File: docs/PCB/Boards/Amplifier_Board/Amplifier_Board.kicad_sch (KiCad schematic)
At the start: 16 parts, among them IC1 LM4871MX_NOPB, J2 Barrel_Jack

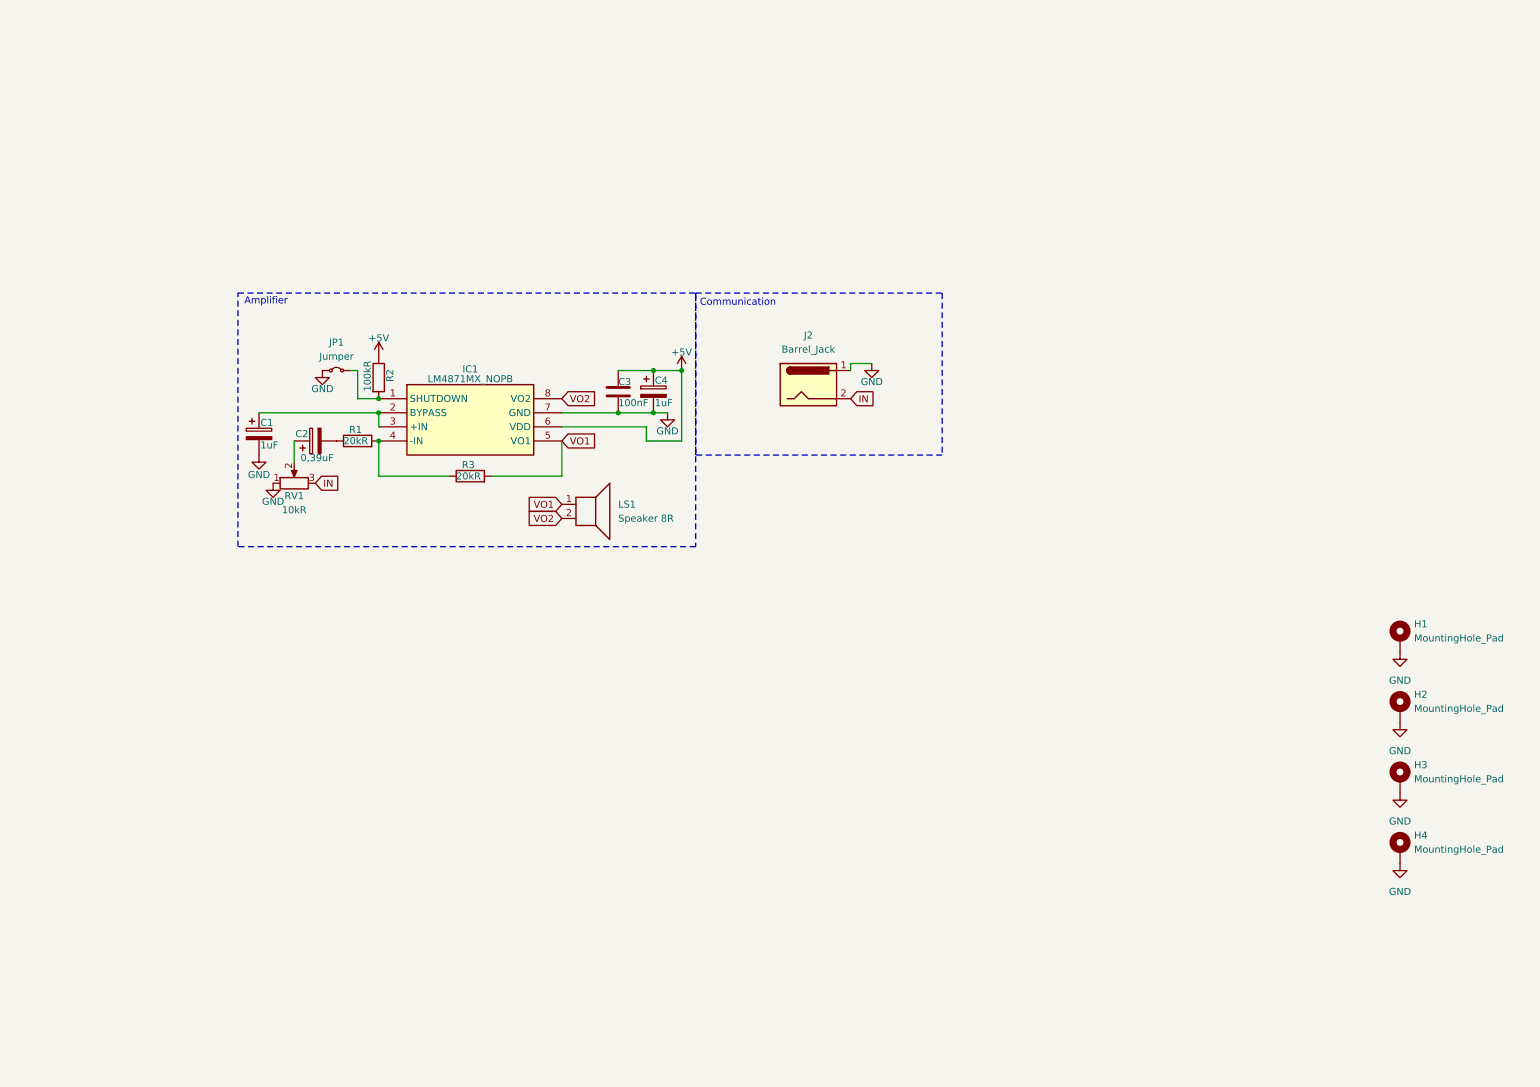
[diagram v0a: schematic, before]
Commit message: Boards modified - tree and power boards added.
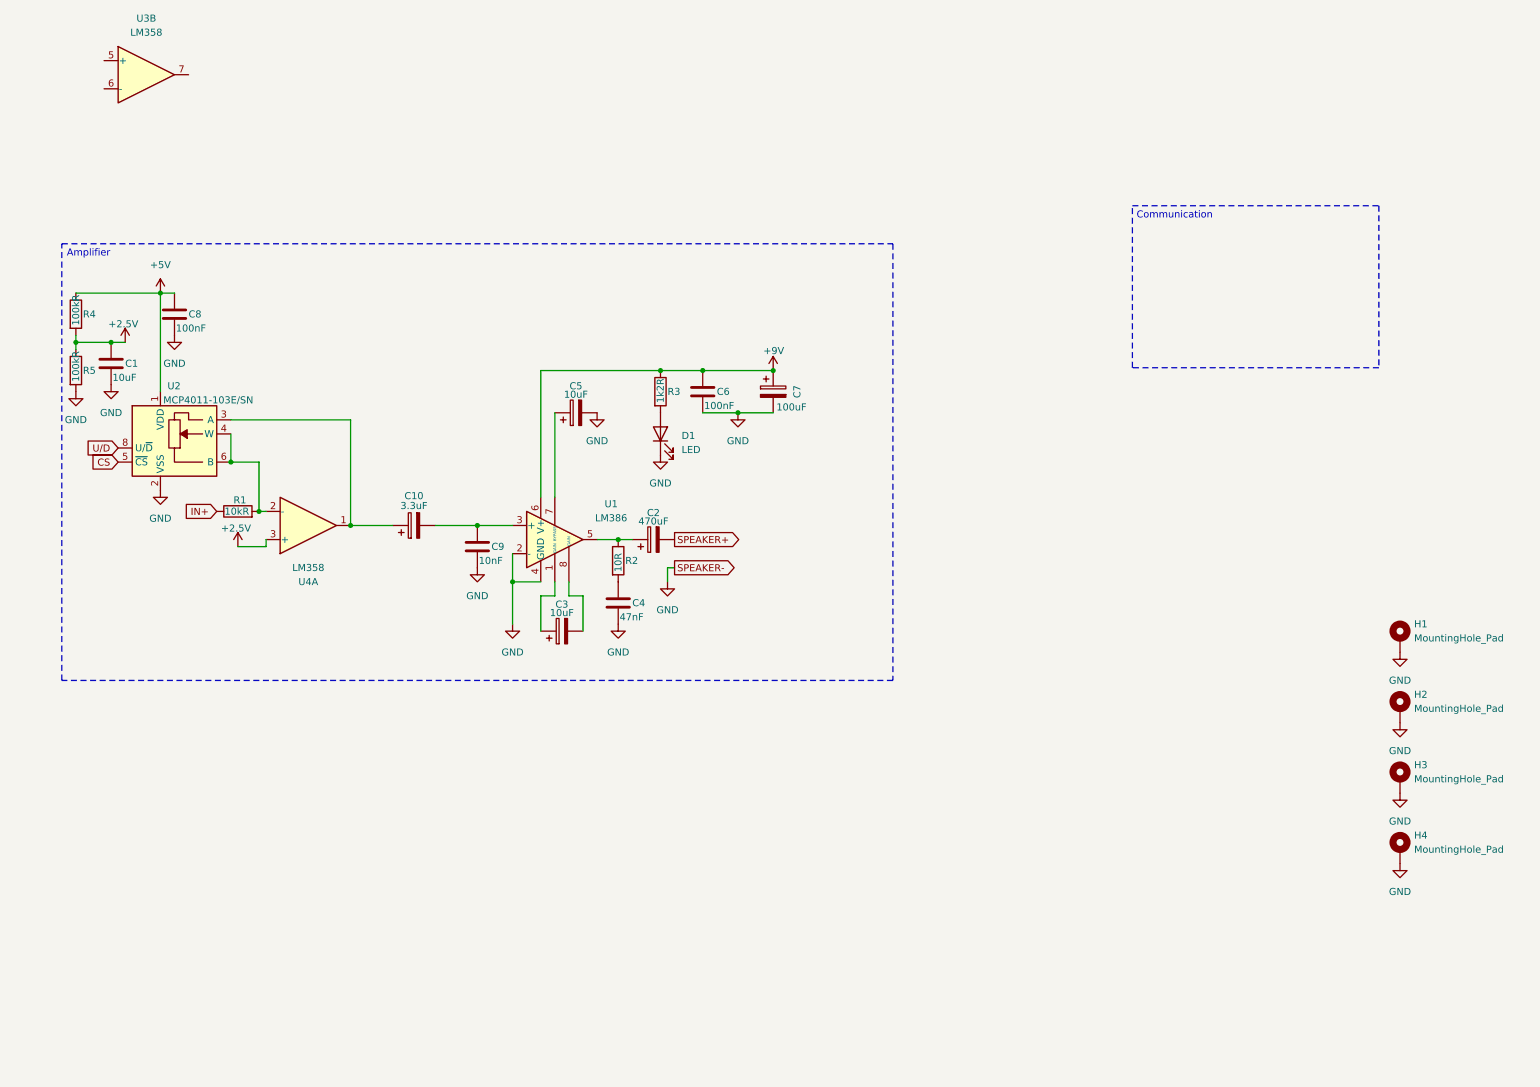
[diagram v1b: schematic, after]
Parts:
- removed C1, C4: 1uF, symbol Device:C_Polarized
- removed C3: 100nF, symbol Device:C
- removed IC1: LM4871MX_NOPB, SOIC127P600X175-8N, symbol Schematy:LM4871MX_NOPB
- removed J2: Barrel_Jack, symbol Connector:Barrel_Jack
- removed JP1: Jumper, symbol Jumper:Jumper_2_Small_Bridged
- removed LS1: Speaker 8R, symbol Device:Speaker
- removed RV1: 10kR, symbol Device:R_Potentiometer
- added C1: 10uF, symbol Device:C
- added C10: 3.3uF, symbol Device:C_Polarized
- added C3, C5: 10uF, symbol Device:C_Polarized
- added C4: 47nF, symbol Device:C
- added C6, C8: 100nF, symbol Device:C
- added C7: 100uF, symbol Device:C_Polarized
- added C9: 10nF, symbol Device:C
- added D1: LED, symbol Device:LED
- added R4, R5: 100kR, symbol Device:R
- added U1: LM386, symbol Amplifier_Audio:LM386
- added U2: MCP4011-103E/SN, Package_SO:SOIC-8_3.9x4.9mm_P1.27mm, symbol Potentiometer_Digital:MCP4011-xxxxSN
- added U3, U4: LM358, symbol Amplifier_Operational:LM358
- C2: value 0,39uF -> 470uF
- R1: value 20kR -> 10kR
- R2: value 100kR -> 10R
- R3: value 20kR -> 1k2R
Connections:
- net +5V: now also C8.1, R4.1, U2.1 (VDD); no longer R2.1
- net GND: now also C1.2, C4.2, C5.2, C6.2, C7.2, C8.2, C9.2, D1.1 (K), R5.2, U1.2 (-), U1.4 (GND), U2.2 (VSS)
- net at R1.2: now also U2.4 (W), U2.6 (B), U4.2 (-); no longer R3.1
- net at C2.1: now also R2.1, U1.5
- net IN+: now reaches R1.1
- net IN+: no longer C2.2
- net at R2.2: now also C4.1
- net VO1: no longer names the net of R3.2
- net VO1: now also D1.2 (A)
- new net: C3.1, U1.1 (GAIN)
- new net: C3.2, U1.8 (GAIN)
- new net: C10.1, U2.3 (A), U4.1
- new net: C10.2, C9.1, U1.3 (+)
- new net: C5.1, U1.7 (BYPASS)
- new net +2.5V: C1.1, R4.2, R5.1, U4.3 (+)
- new net +9V: C6.1, C7.1, R3.1, U1.6 (V+)
- new net CS: U2.5 (~{CS})
- new net SPEAKER+: C2.2
- new net U/D: U2.8 (U/~{D})

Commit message: Amplifier board added,base pico programs added.
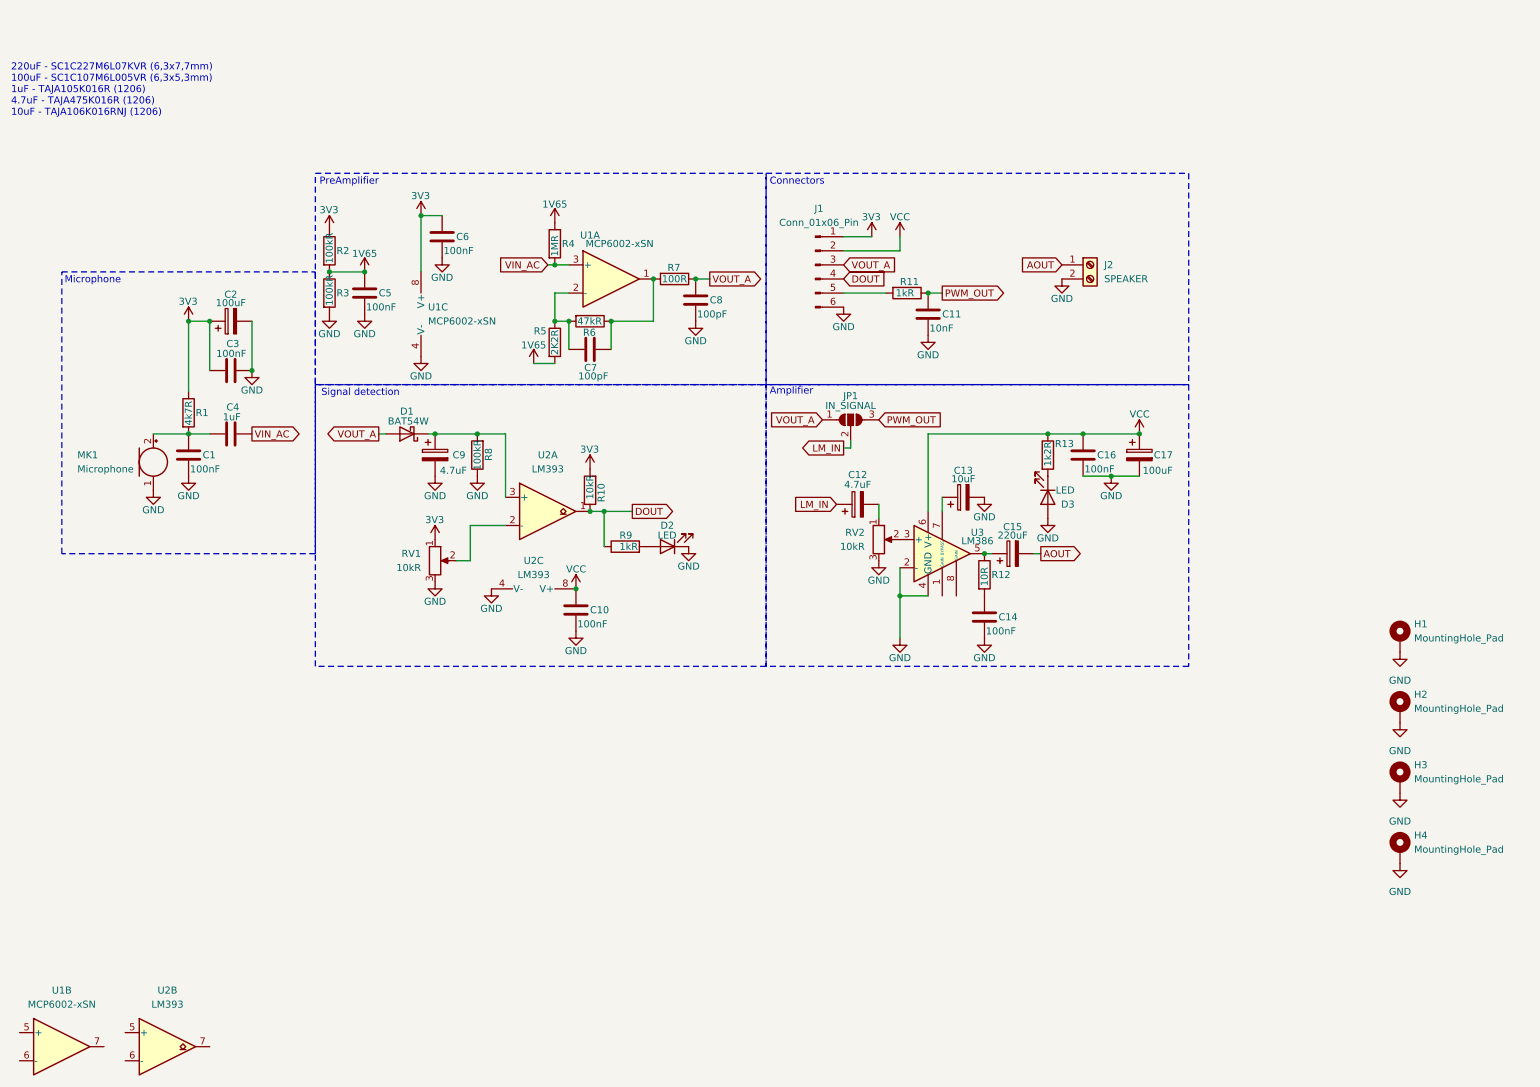
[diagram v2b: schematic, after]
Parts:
- removed C3: 10uF, symbol Device:C_Polarized
- removed C9: 10nF, symbol Device:C
- removed U2: MCP4011-103E/SN, Package_SO:SOIC-8_3.9x4.9mm_P1.27mm, symbol Potentiometer_Digital:MCP4011-xxxxSN
- removed U3, U4: LM358, symbol Amplifier_Operational:LM358
- added C10, C3, C5, C6: 100nF, Capacitor_SMD:C_0805_2012Metric, symbol Device:C
- added C11: 10nF, Capacitor_SMD:C_0805_2012Metric, symbol Device:C
- added C2: 100uF, Capacitor_SMD:CP_Elec_6.3x5.3, symbol Device:C_Polarized
- added C4: 1uF, Capacitor_SMD:C_1206_3216Metric, symbol Device:C
- added C7: 100pF, Capacitor_SMD:C_0805_2012Metric, symbol Device:C
- added C9: 4.7uF, Capacitor_SMD:C_1206_3216Metric, symbol Device:C_Polarized
- added D1: BAT54W, Diode_SMD:D_SOD-323F, symbol Device:D_Schottky
- added D2: LED, LED_SMD:LED_0805_2012Metric, symbol Device:LED
- added J1: Conn_01x06_Pin, Connector_PinHeader_2.54mm:PinHeader_1x06_P2.54mm_Vertical, symbol Connector:Conn_01x06_Pin
- added J2: SPEAKER, TerminalBlock_Phoenix:TerminalBlock_Phoenix_MKDS-1,5-2_1x02_P5.00mm_Horizontal, symbol Connector:Screw_Terminal_01x02
- added JP1: IN_SIGNAL, Connector_PinHeader_2.54mm:PinHeader_1x03_P2.54mm_Vertical, symbol Jumper:SolderJumper_3_Open
- added MK1: Microphone, Sensor_Audio:POM-2244P-C3310-2-R, symbol Device:Microphone
- added R10: 10kR, Resistor_SMD:R_0805_2012Metric, symbol Device:R
- added R11, R9: 1kR, Resistor_SMD:R_0805_2012Metric, symbol Device:R
- added R2, R3, R8: 100kR, Resistor_SMD:R_0805_2012Metric, symbol Device:R
- added R6: 47kR, Resistor_SMD:R_0805_2012Metric, symbol Device:R
- added R7: 100R, Resistor_SMD:R_0805_2012Metric, symbol Device:R
- added RV1, RV2: 10kR, Potentiometer_THT:Potentiometer_Runtron_RM-065_Vertical, symbol Device:R_Potentiometer
- added U1: MCP6002-xSN, Package_SO:SOIC-8_3.9x4.9mm_P1.27mm, symbol Amplifier_Operational:MCP6002-xSN
- added U2: LM393, Package_SO:SOIC-8_3.9x4.9mm_P1.27mm, symbol Comparator:LM393
- C1: value 10uF -> 100nF; footprint (none) -> Capacitor_SMD:C_0805_2012Metric
- C12: renamed from C10; value 3.3uF -> 4.7uF; footprint (none) -> Capacitor_SMD:C_1206_3216Metric
- C13: renamed from C5; footprint (none) -> Capacitor_SMD:C_1206_3216Metric
- C14: renamed from C4; value 47nF -> 100nF; footprint (none) -> Capacitor_SMD:C_0805_2012Metric
- C15: renamed from C2; value 470uF -> 220uF; footprint (none) -> Capacitor_SMD:CP_Elec_6.3x7.7
- C16: renamed from C6; footprint (none) -> Capacitor_SMD:C_0805_2012Metric
- C17: renamed from C7; footprint (none) -> Capacitor_SMD:CP_Elec_6.3x5.3
- C8: value 100nF -> 100pF; footprint (none) -> Capacitor_SMD:C_0805_2012Metric
- D3: renamed from D1; footprint (none) -> LED_SMD:LED_0805_2012Metric
- R1: value 10kR -> 4k7R; footprint (none) -> Resistor_SMD:R_0805_2012Metric
- R12: renamed from R2; footprint (none) -> Resistor_SMD:R_0805_2012Metric
- R13: renamed from R3; footprint (none) -> Resistor_SMD:R_0805_2012Metric
- R4: value 100kR -> 1MR; footprint (none) -> Resistor_SMD:R_0805_2012Metric
- R5: value 100kR -> 2K2R; footprint (none) -> Resistor_SMD:R_0805_2012Metric
- U3: renamed from U1; footprint (none) -> Package_SO:SOIC-8_3.9x4.9mm_P1.27mm
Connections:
- net GND: now also D3.2 (A), C10.2, C11.2, C2.2, C3.1, C5.2, C6.2, C9.2, D2.1 (K), J1.6 (Pin_6), J2.2 (Pin_2), MK1.1 (-), R3.2, R8.1, RV1.3, RV2.3, U1.4 (V-), U2.4 (V-); no longer D3.1 (K), R5.2
- net at R1.2: now also C1.1, C4.2, MK1.2 (+)
- net at R13.2: now also D3.1 (K); no longer D3.2 (A)
- net LM_IN: now reaches C12.1
- net LM_IN: now also JP1.2 (C)
- net at U3.3 (+): now also RV2.2; no longer C12.2
- removed net +2.5V: C1.1, R4.2, R5.1
- net +5V renamed 1V65
- net 1V65: now also R5.2, C5.1, R2.2, R3.1; no longer C8.1
- net +9V renamed VCC
- net VCC: now also C10.1, J1.2 (Pin_2), U2.8 (V+)
- net IN+ renamed 3V3
- net 3V3: now also C2.1, C3.2, C6.1, J1.1 (Pin_1), R10.2, R2.1, RV1.1, U1.8 (V+)
- net SPEAKER+ renamed AOUT
- net AOUT: now also J2.1 (Pin_1)
- new net: C7.2, R6.1, R7.2, U1.1
- new net: C7.1, R5.1, R6.2, U1.2 (-)
- new net: RV1.2, U2.2 (-)
- new net: J1.5 (Pin_5), R11.2
- new net: C9.1, D1.1 (K), R8.2, U2.3 (+)
- new net: C12.2, RV2.1
- new net: D2.2 (A), R9.2
- new net DOUT: J1.4 (Pin_4), R10.1, R9.1, U2.1
- new net PWM_OUT: C11.1, JP1.3 (B), R11.1
- new net VIN_AC: C4.1, R4.2, U1.3 (+)
- new net VOUT_A: C8.1, D1.2 (A), J1.3 (Pin_3), JP1.1 (A), R7.1
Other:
- note added: "220uF - SC1C227M6L07KVR (6,3x7,7mm) 100uF - SC1C107M6L005VR (6,3x5,3mm) 1uF - TAJA105K016R (1206) 4.7uF - TAJA475K016R (1206) 10uF - TAJA106K016RNJ (1206)"
- note added: "Connectors"
- note added: "Microphone"
- note added: "PreAmplifier"
- note added: "Signal detection"
- note removed: "Communication"
- moved on the sheet: C12, C13, C14, C15, C16, C17, D3, R12, R13, U3

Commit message: Code review
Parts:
- added C18: 47nF, Capacitor_SMD:C_0805_2012Metric, symbol Device:C
- added D4, D5: 1N4148W, Diode_SMD:D_SOD-123, symbol Diode:1N4148W
- added R14, R15: 1kR, Resistor_SMD:R_0805_2012Metric, symbol Device:R
- J1: value Conn_01x06_Pin -> CON
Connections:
- net 3V3: now also D5.1 (K)
- net GND: now also C18.2, D4.2 (A)
- net PWM_OUT: now also C18.1, R15.1; no longer C11.1, R11.1
- net VOUT_A: now also R14.1; no longer J1.3 (Pin_3)
- new net: D4.1 (K), D5.2 (A), J1.3 (Pin_3), R14.2
- new net: C11.1, R11.1, R15.2
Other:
- moved on the sheet: C11, J1, J2, R11

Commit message: Boards modified.
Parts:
- C1: value 100nF -> 10nF
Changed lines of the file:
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@@
 			)
 		)
-		(property "Value" "100nF"
+		(property "Value" "10nF"
 			(at 45.974 86.36 0)
 			(effects
